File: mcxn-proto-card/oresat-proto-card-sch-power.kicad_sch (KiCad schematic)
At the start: 89 parts, among them Q1 DMP2240UDM, Q2 DMP3050LVT-7, Q7 MOSFET-PCH-SOT23-6, Q8 PMV45EN, Q9 PMV45EN, U10 TPS62111RSA, U11 MIC842LYC5, U12 MIC842LYC5, U2 MAX7310, U3 TS5A21366DCUR, U6 MAX4211

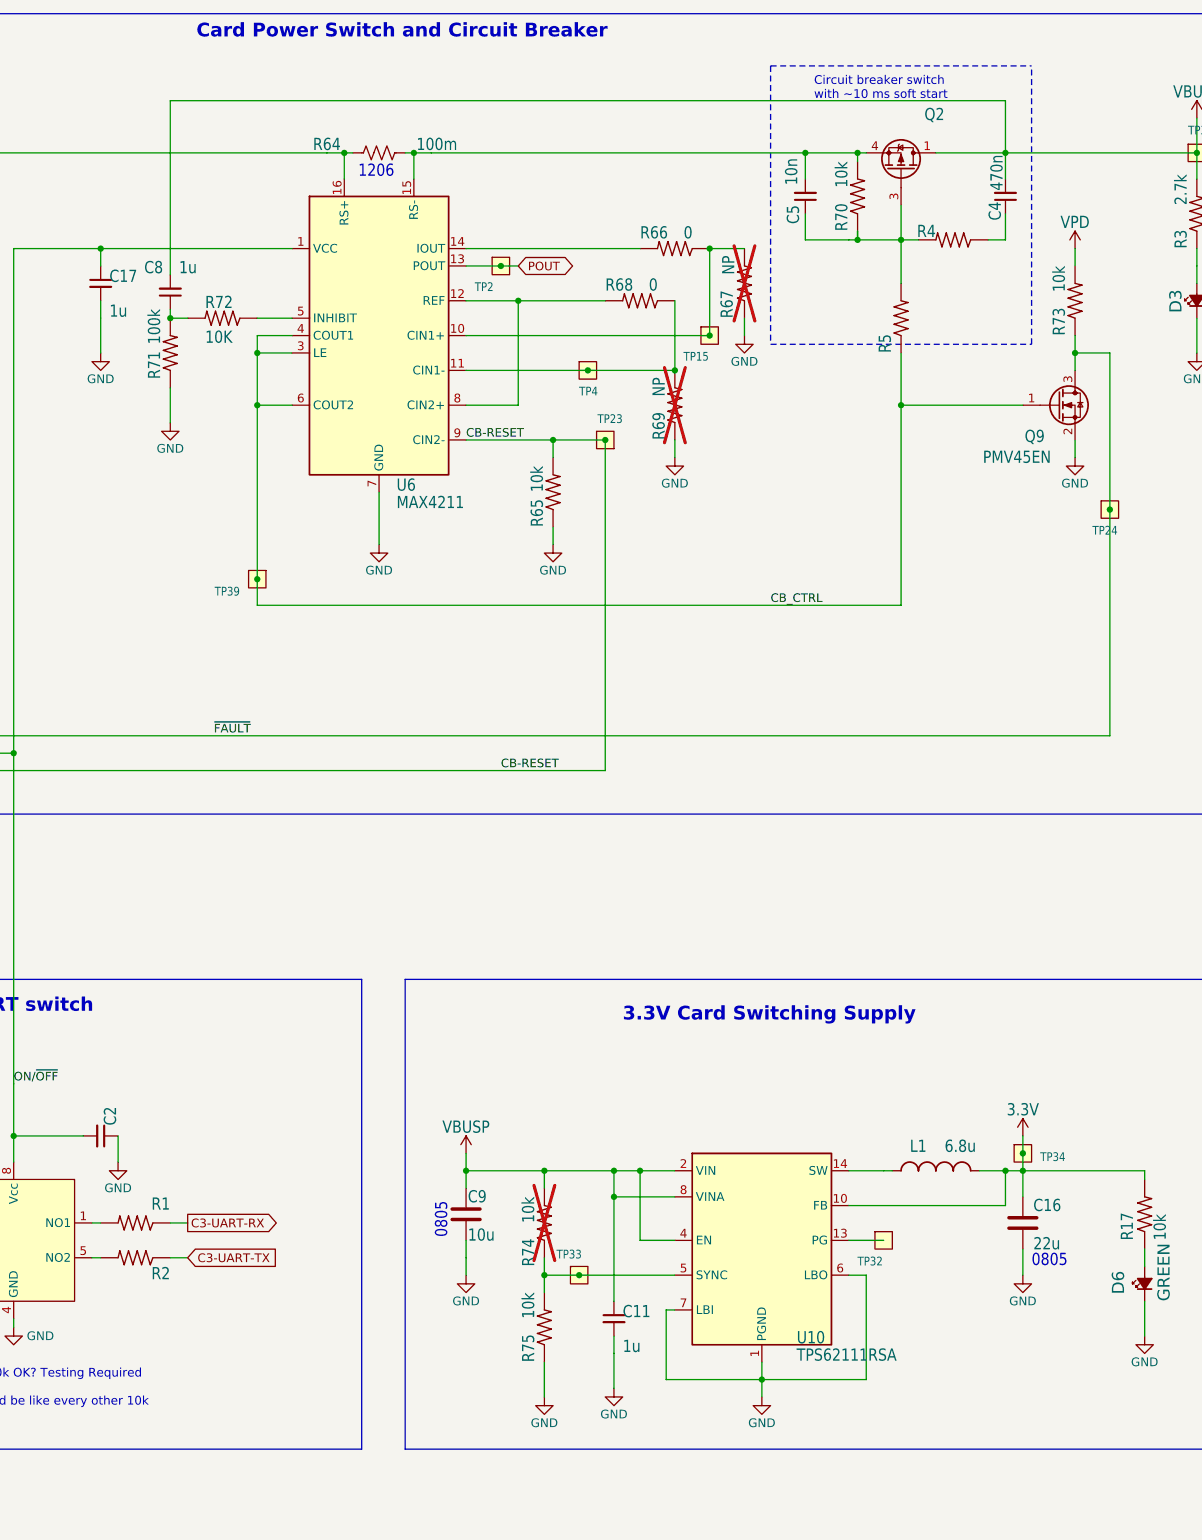
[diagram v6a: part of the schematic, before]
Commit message: Fixed linked library footprints and routing
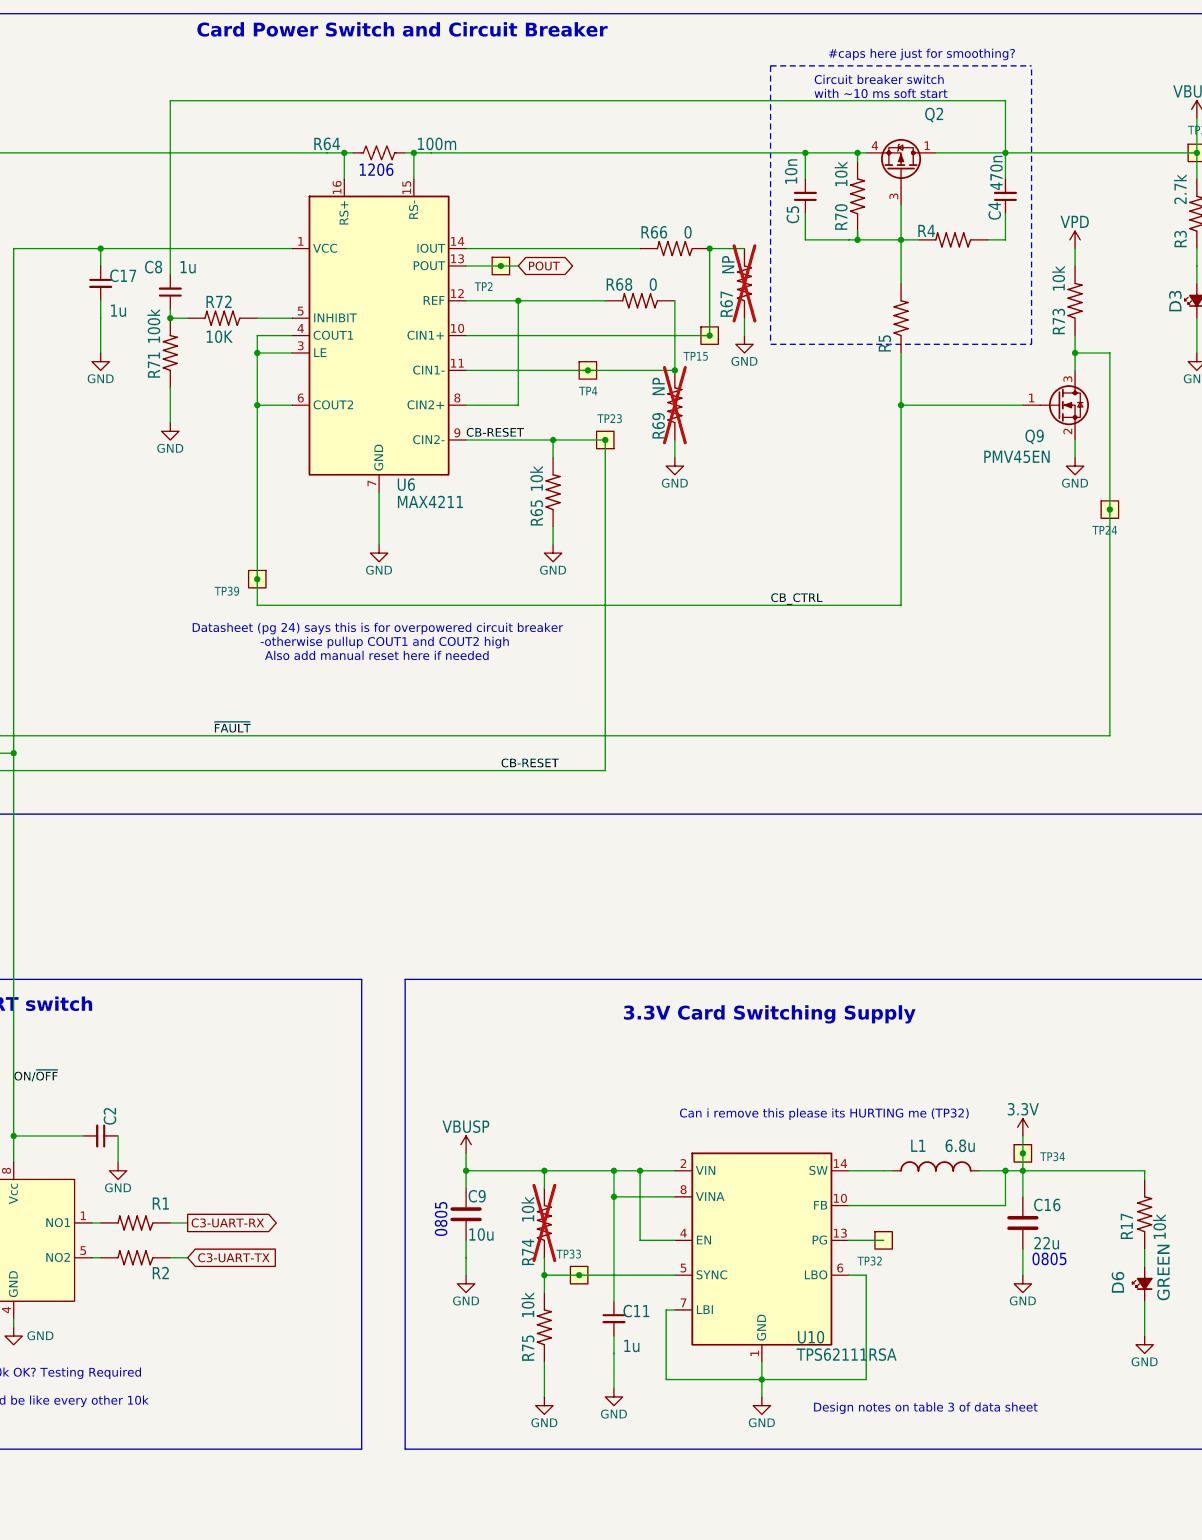
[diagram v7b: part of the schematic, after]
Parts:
- L1: footprint oresat-proto-card:ECS-MPI4040 -> oresat-passives:L_ECS-MPI4040
- Q2, Q7: footprint Package_TO_SOT_SMD:SOT-23-6 -> Package_TO_SOT_SMD:TSOT-23-6
- Q8: footprint oresat-ics:SOT23 -> Package_TO_SOT_SMD:SOT-23
- Q9: footprint oresat-proto-card:SOT23 -> Package_TO_SOT_SMD:SOT-23
- R64: footprint oresat-passives:1206-C -> Resistor_SMD:R_1206_3216Metric
- U10: footprint Package_DFN_QFN:QFN-16-1EP_4x4mm_P0.65mm_EP2.15x2.15mm -> Package_DFN_QFN:Texas_RSA_VQFN-16-1EP_4x4mm_P0.65mm_EP2.7x2.7mm
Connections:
- net AGND renamed GND
- net GND: now also U10.17 (GND)
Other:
- note added: "#caps here just for smoothing?"
- note added: "Can i remove this please its HURTING me (TP32)"
- note added: "Datasheet (pg 24) says this is for overpowered circuit breaker -otherwise pullup COUT1 and COUT2 high Also add manual reset here if needed"
- note added: "Design notes on table 3 of data sheet"
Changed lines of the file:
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@@
 		)
 	)
+	(text "Can i remove this please its HURTING me (TP32)"
+		(exclude_from_sim no)
+		(at 352.044 176.022 0)
+		(effects
+			(font
+				(size 1.27 1.27)
+			)
+		)
+	)
 	(text "IS 10k OK? Testing Required\n\nShould be like every other 10k"
 		(exclude_from_sim no)
@@
 		)
 	)
+	(text "Datasheet (pg 24) says this is for overpowered circuit breaker\n	-otherwise pullup COUT1 and COUT2 high\nAlso add manual reset here if needed"
+		(exclude_from_sim no)
+		(at 286.766 107.188 0)
+		(effects
+			(font
+				(size 1.27 1.27)
+			)
+		)
+	)
+	(text "#caps here just for smoothing?"
+		(exclude_from_sim no)
+		(at 366.268 21.336 0)
+		(effects
+			(font
+				(size 1.27 1.27)
+			)
+		)
+	)
 	(text "0805"
 		(exclude_from_sim no)
@@
 		)
 	)
+	(text "Design notes on table 3 of data sheet"
+		(exclude_from_sim no)
+		(at 366.776 218.948 0)
+		(effects
+			(font
+				(size 1.27 1.27)
+			)
+		)
+	)
 	(text "Main Power Switch"
 		(exclude_from_sim no)
@@
 			)
 		)
-		(property "Footprint" "oresat-proto-card:SOT23"
+		(property "Footprint" "Package_TO_SOT_SMD:SOT-23"
 			(at 391.16 69.85 0)
 			(effects
@@
 			)
 		)
-		(property "Datasheet" "~"
+		(property "Datasheet" "https://assets.nexperia.com/documents/data-sheet/PMV45EN2.pdf"
 			(at 386.08 72.39 0)
 			(effects
@@
 			)
 		)
-		(property "Footprint" "Package_DFN_QFN:QFN-16-1EP_4x4mm_P0.65mm_EP2.15x2.15mm"
+		(property "Footprint" "Package_DFN_QFN:Texas_RSA_VQFN-16-1EP_4x4mm_P0.65mm_EP2.7x2.7mm"
 			(at 342.9 191.77 0)
 			(effects
@@
 			)
 		)
-		(property "Datasheet" "https://www.ti.com/lit/ds/symlink/tps62110.pdf?HQS=dis-dk-null-digikeymode-dsf-pf-null-wwe&ts=1751434366274&ref_url=https%253A%252F%252Fwww.ti.com%252Fgeneral%252Fdocs%252Fsuppproductinfo.tsp%253FdistId%253D10%2526gotoUrl%253Dhttps%253A%252F%252Fwww.ti.com%252Flit%252Fgpn%252Ftps62110"
+		(property "Datasheet" "https://www.ti.com/lit/ds/symlink/tps62110.pdf?ts=1752185757661&ref_url=https%253A%252F%252Fwww.google.com%252F"
 			(at 342.9 191.77 0)
 			(effects
@@
 		(pin "3"
 		)
+		(pin "17"
+		)
 		(instances
 			(project "oresat-proto-card"
@@
 			)
 		)
-		(property "Footprint" "oresat-proto-card:ECS-MPI4040"
+		(property "Footprint" "oresat-passives:L_ECS-MPI4040"
 			(at 368.3 184.15 0)
 			(effects
@@
 			)
 		)
-		(property "Footprint" "Package_TO_SOT_SMD:SOT-23-6"
+		(property "Footprint" "Package_TO_SOT_SMD:TSOT-23-6"
 			(at 361.315 33.02 0)
 			(effects
@@
 			)
 		)
-		(property "Description" "P-Channel Power MOSFET, SOT-23-6"
+		(property "Description" "P-Channel Power MOSFET, TSOT-23-6"
 			(at 363.22 38.1 0)
 			(effects
@@
 			)
 		)
-		(property "Footprint" "oresat-ics:SOT23"
+		(property "Footprint" "Package_TO_SOT_SMD:SOT-23"
 			(at 209.55 53.34 0)
 			(effects
@@
 			)
 		)
-		(property "Datasheet" "~"
+		(property "Datasheet" "https://assets.nexperia.com/documents/data-sheet/PMV45EN2.pdf"
 			(at 204.47 55.88 0)
 			(effects
@@
 			)
 		)
-		(property "Footprint" "Package_TO_SOT_SMD:SOT-23-6"
+		(property "Footprint" "Package_TO_SOT_SMD:TSOT-23-6"
 			(at 208.915 33.02 0)
 			(effects
@@
 			)
 		)
-		(property "Description" "P-Channel Power MOSFET, SOT-23-6"
+		(property "Description" "P-Channel Power MOSFET, TSOT-23-6"
 			(at 210.82 38.1 0)
 			(effects
@@
 			)
 		)
-		(property "Footprint" "oresat-passives:1206-C"
+		(property "Footprint" "Resistor_SMD:R_1206_3216Metric"
 			(at 287.02 35.56 0)
 			(effects

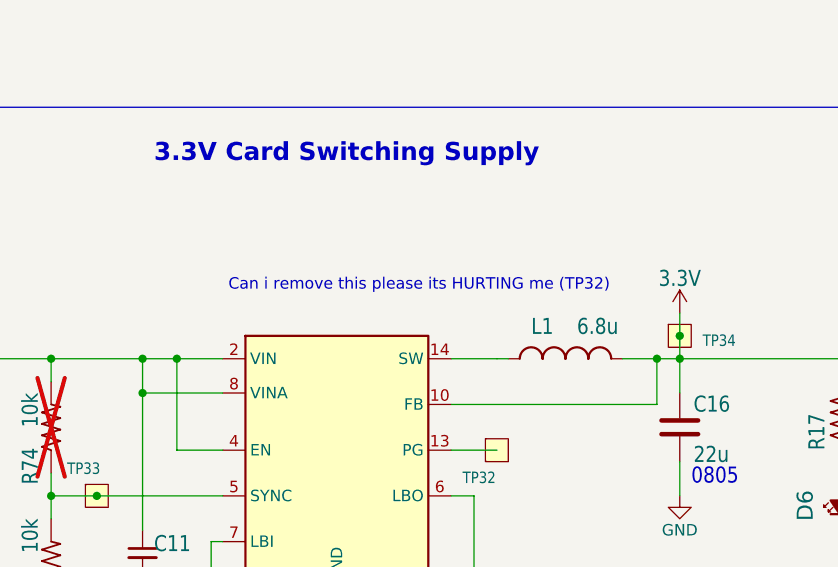
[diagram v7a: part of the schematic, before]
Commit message: Fixed schematic and routing for 2x11 connector
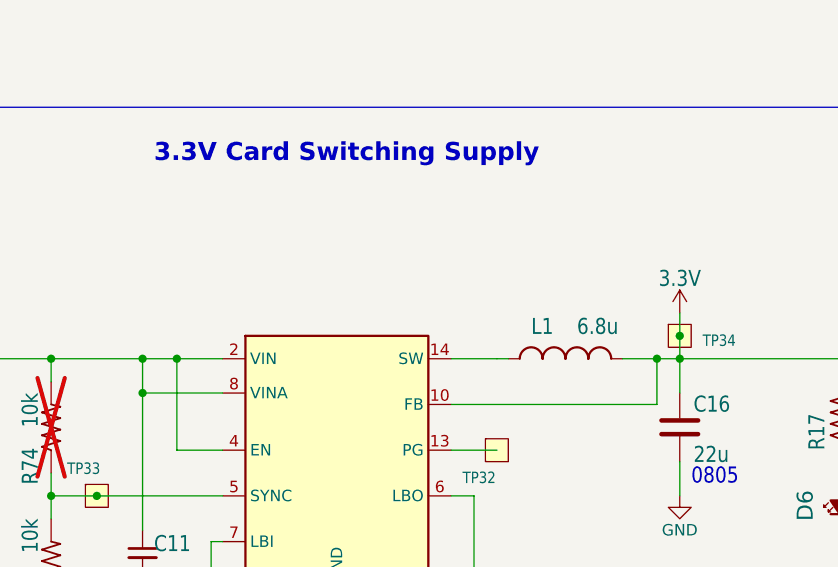
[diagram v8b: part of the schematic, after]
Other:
- note removed: "Can i remove this please its HURTING me (TP32)"
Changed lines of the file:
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@@
-		)
-	)
-	(text "Can i remove this please its HURTING me (TP32)"
-		(exclude_from_sim no)
-		(at 352.044 176.022 0)
-		(effects
-			(font
-				(size 1.27 1.27)
-			)
 		)
 	)
